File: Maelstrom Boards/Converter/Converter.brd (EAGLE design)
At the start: 101.6 x 101.6 mm, 1 part

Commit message: converter work
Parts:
- added 12VCONVERTER, 3.3VCONVERTER, 5VCONVERTER: CONVERTER, converter:CONVERTER
- added BALANCEDRAWIN: 39-30-06?, con-molex-mini-fit:39-30-?06?
- added C1, C12, C7: (no value), rcl:E3,5-10
- added C10, C13, C14, C15, C3, C4, C5, C8, C9: (no value), resistor:C1206K
- added C11, C2, C6: (no value), rcl:E5-13
- added DIAMOND: 43045-08, con-molex-micro-fit:43045-08
- added JETSON, PNUEMATICS: 39-30-02?, con-molex-mini-fit:39-30-?02?
- added L1, L2, L3: (no value), rcl:POWER-CHOKE_WE-TPC
- added Q1, Q2, Q3: BSS295, transistor-fet:TO92
- added R4: 4.47 K, rcl:0207/10
- added R5: 1.41 K, rcl:0207/10
- added R6: 7.6 K, rcl:0207/10
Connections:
- new net +12V: 12VCONVERTER.7,SENSE+, 12VCONVERTER.8,VOUT(+)
- new net +3V3: 3.3VCONVERTER.7,SENSE+, 3.3VCONVERTER.8,VOUT(+), U$1.4, U$1.5, U$1.51, U$1.52, U$1.53, U$1.6
- new net +5V: 5VCONVERTER.7,SENSE+, 5VCONVERTER.8,VOUT(+), U$1.1, U$1.2, U$1.3, U$1.54, U$1.55, U$1.56
- new net 12VCURRENTOUT: C3.1, C4.1, C5.1, DIAMOND.1, DIAMOND.2, DIAMOND.3, DIAMOND.4, JETSON.1, PNUEMATICS.1
- new net 12VFILTERED+: 12VCONVERTER.1,VIN(+)
- new net 12VON: Q1.1, U$1.21
- new net 3.3VFILTERED+: 3.3VCONVERTER.1,VIN(+)
- new net 3.3VON: Q3.1, U$1.23
- new net 5VFILTERED+: 5VCONVERTER.1,VIN(+)
- new net 5VON: Q2.1, U$1.22
- new net AGND: 12VCONVERTER.3,VIN(-)/GND, 12VCONVERTER.4,VOUT(-)/GND, 3.3VCONVERTER.3,VIN(-)/GND, 3.3VCONVERTER.4,VOUT(-)/GND, 5VCONVERTER.3,VIN(-)/GND, 5VCONVERTER.4,VOUT(-)/GND, Q1.3, Q2.3, Q3.3, R4.1, R5.1, R6.1, U$1.48, U$1.49, U$1.50, U$1.7, U$1.8, U$1.9
- new net BALANCED+: BALANCEDRAWIN.1, BALANCEDRAWIN.2, BALANCEDRAWIN.3, C1.+, C12.+, C7.+, L1.1, L2.1, L3.1
- new net BALANCED-: BALANCEDRAWIN.4, BALANCEDRAWIN.5, BALANCEDRAWIN.6, C1.-, C11.-, C12.-, C2.-, C6.-, C7.-
- new net CMGND: C3.2, C4.2, C5.2, DIAMOND.5, DIAMOND.6, DIAMOND.7, DIAMOND.8, JETSON.2, PNUEMATICS.2
- new net N$1: 5VCONVERTER.6,TRIM, R4.2
- new net N$10: C13.1, C14.1, C15.1
- new net N$11: C13.2, C14.2, C15.2
- new net N$13: 12VCONVERTER.2,ON/OFF, Q1.2
- new net N$16: 5VCONVERTER.2,ON/OFF, Q2.2
- new net N$17: 3.3VCONVERTER.6,TRIM, R6.2
- new net N$19: 3.3VCONVERTER.2,ON/OFF, Q3.2
- new net N$2: 12VCONVERTER.6,TRIM, R5.2
- new net N$3: C2.+, L1.2
- new net N$5: C6.+, L2.2
- new net N$6: C10.1, C8.1, C9.1
- new net N$7: C10.2, C8.2, C9.2
- new net N$9: C11.+, L3.2

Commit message: Converter work
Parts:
- added R1: 10K, rcl:R0603
- added R2: 1.41 K, rcl:R0603
- added R3, R7, R8, R9: 4.47 K, rcl:R0603
- C1, C7: value (none) -> 1000 uF
- C10, C13, C14, C15, C3, C4, C5, C8, C9: value (none) -> 47 uF
- C11, C2, C6: value (none) -> 330 uF; device rcl:E5-13 -> rcl:E3,5-8
- C12: value (none) -> 1000
- L1, L2, L3: value (none) -> 1 uH
- R4, R5, R6: device rcl:0207/10 -> rcl:R0603
- moved Q3 267.6 mm to (70.4, 82.3)
- moved Q1 264.1 mm to (70.1, 88.4)
- moved R6 263.2 mm to (79.8, 83.1)
- moved 12VCONVERTER 241.2 mm to (30.5, 71.1)
- moved R5 232.3 mm to (80.7, 47.3)
- moved R4 210.5 mm to (75.2, 58.9)
- moved Q2 206.2 mm to (82.6, 29.5)
- moved L3 173.5 mm to (83.2, 64.1)
- moved C7 172.9 mm to (7.83, 92.9)
- moved L1 170.7 mm to (24.6, 91.1), turned to 270 degrees
- moved 3.3VCONVERTER 168.6 mm to (30.5, 45.7)
- moved 5VCONVERTER 167.2 mm to (30.5, 20.3)
- moved C13 156.4 mm to (72.3, 43.7)
- moved C14 156.4 mm to (77.0, 43.7)
- moved C15 156.4 mm to (81.7, 43.7)
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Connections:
- net N$1 renamed 5VTRIM
- net N$10 renamed +3.3V
- net N$13 renamed 12VON-CON
- net N$16 renamed 5VON-CON
- net N$17 renamed 3.3VTRIM
- net N$19 renamed 3.3VON-CON
- net N$2 renamed 12VTRIM
- removed net 12VCURRENTOUT: C3.1, C4.1, C5.1, DIAMOND.1, DIAMOND.2, DIAMOND.3, DIAMOND.4, JETSON.1, PNUEMATICS.1
- removed net CMGND: C3.2, C4.2, C5.2, DIAMOND.5, DIAMOND.6, DIAMOND.7, DIAMOND.8, JETSON.2, PNUEMATICS.2
- removed net N$11: C13.2, C14.2, C15.2
- removed net N$3: C2.+, L1.2
- removed net N$5: C6.+, L2.2
- removed net N$6: C10.1, C8.1, C9.1
- removed net N$7: C10.2, C8.2, C9.2
- removed net N$9: C11.+, L3.2
- net +12V: now also C3.1, C4.1, C5.1, DIAMOND.1, DIAMOND.2, DIAMOND.3, DIAMOND.4, JETSON.1, PNUEMATICS.1
- net +5V: now also C10.1, C8.1, C9.1
- net 12VFILTERED+: now also C2.+, L1.2
- net 12VON: now also R1.1, R2.2
- net 3.3VFILTERED+: now also C11.+, L3.2
- net 3.3VON: now also R8.1, R9.2
- net 5VFILTERED+: now also C6.+, L2.2
- net 5VON: now also R3.1, R7.2
- net AGND: now also C10.2, C13.2, C14.2, C15.2, C3.2, C4.2, C5.2, C8.2, C9.2, DIAMOND.5, DIAMOND.6, DIAMOND.7, DIAMOND.8, JETSON.2, PNUEMATICS.2, R2.1, R7.1, R9.1
- net BALANCED+: now also R1.2, R3.2, R8.2

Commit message: Converter board
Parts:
- R2: value 1.41 K -> 1.35K
- R3, R8: value 4.47 K -> 10K
- R7, R9: value 4.47 K -> 1.35K
- moved R9 206.4 mm to (18.2, 57.7)
- moved R8 202.0 mm to (27.6, 57.1), turned to 90 degrees
- moved R2 193.8 mm to (19.0, 80.1), turned to 90 degrees
- moved R1 181.5 mm to (25.7, 79.6), turned to 270 degrees
- moved R7 171.0 mm to (28.9, 30.4)
- moved R3 158.0 mm to (24.3, 30.6), turned to 90 degrees
- moved DIAMOND 140.9 mm to (91.2, 68.5), turned to 90 degrees
- moved PNUEMATICS 136.4 mm to (87.4, 52.7), turned to 90 degrees
- moved JETSON 120.4 mm to (87.2, 84.8), turned to 90 degrees
- moved L2 60.8 mm to (22.4, 48.0), turned to 0 degrees
- moved L3 59.0 mm to (24.2, 63.5), turned to 180 degrees
- moved Q2 49.4 mm to (33.2, 30.6)
- moved Q3 44.1 mm to (34.8, 56.2)
- moved C7 42.0 mm to (8.24, 50.9), turned to 270 degrees
- moved Q1 36.1 mm to (35.1, 79.7)
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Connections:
- removed net BALANCED-: BALANCEDRAWIN.4, BALANCEDRAWIN.5, BALANCEDRAWIN.6, C1.-, C11.-, C12.-, C2.-, C6.-, C7.-
- net AGND: now also BALANCEDRAWIN.4, BALANCEDRAWIN.5, BALANCEDRAWIN.6, C1.-, C11.-, C12.-, C2.-, C6.-, C7.-
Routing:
- net AGND: track 0.00 -> 1.40 mm, vias 0 -> 1
- added copper zone on layer 16, net AGND
- added copper zone on layer 1, net BALANCED+

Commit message: Converter board work
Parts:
- moved R9 4.44 mm to (22.6, 57.2), turned to 270 degrees
- moved R2 1.37 mm to (20.2, 79.6)
- moved R7 0.83 mm to (28.1, 30.6), turned to 270 degrees
- moved Q1 0.76 mm to (34.4, 79.7)
- moved Q2 0.76 mm to (34.0, 30.6)
- moved Q3 0.51 mm to (34.3, 56.2)
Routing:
- net AGND: track 1.40 -> 5.37 mm, vias 1 -> 3

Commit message: Converter layout finished
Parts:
- moved C15 60.0 mm to (26.3, 20.8), turned to 180 degrees
- moved C10 57.7 mm to (18.9, 20.9), turned to 180 degrees
- moved C9 57.3 mm to (18.9, 17.6), turned to 180 degrees
- moved C14 57.0 mm to (26.3, 17.6), turned to 180 degrees
- moved C8 56.9 mm to (18.9, 14.3), turned to 180 degrees
- moved C13 54.6 mm to (26.3, 14.3), turned to 180 degrees
- moved C3 48.8 mm to (83.6, 62.3), turned to 180 degrees
- moved C4 47.7 mm to (83.6, 65.9), turned to 180 degrees
- moved C5 46.6 mm to (83.6, 69.4), turned to 180 degrees
- moved R5 36.8 mm to (75.4, 83.8), turned to 180 degrees
- moved R4 26.0 mm to (75.4, 32.9), turned to 180 degrees
- moved R6 25.1 mm to (75.4, 58.3), turned to 180 degrees
- moved R3 4.64 mm to (28.8, 31.4)
- moved L2 3.88 mm to (26.1, 46.6), turned to 90 degrees
- moved R2 3.31 mm to (23.5, 80.4), turned to 270 degrees
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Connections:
- removed net +3.3V: C13.1, C14.1, C15.1
- net +3V3: now also C13.1, C14.1, C15.1

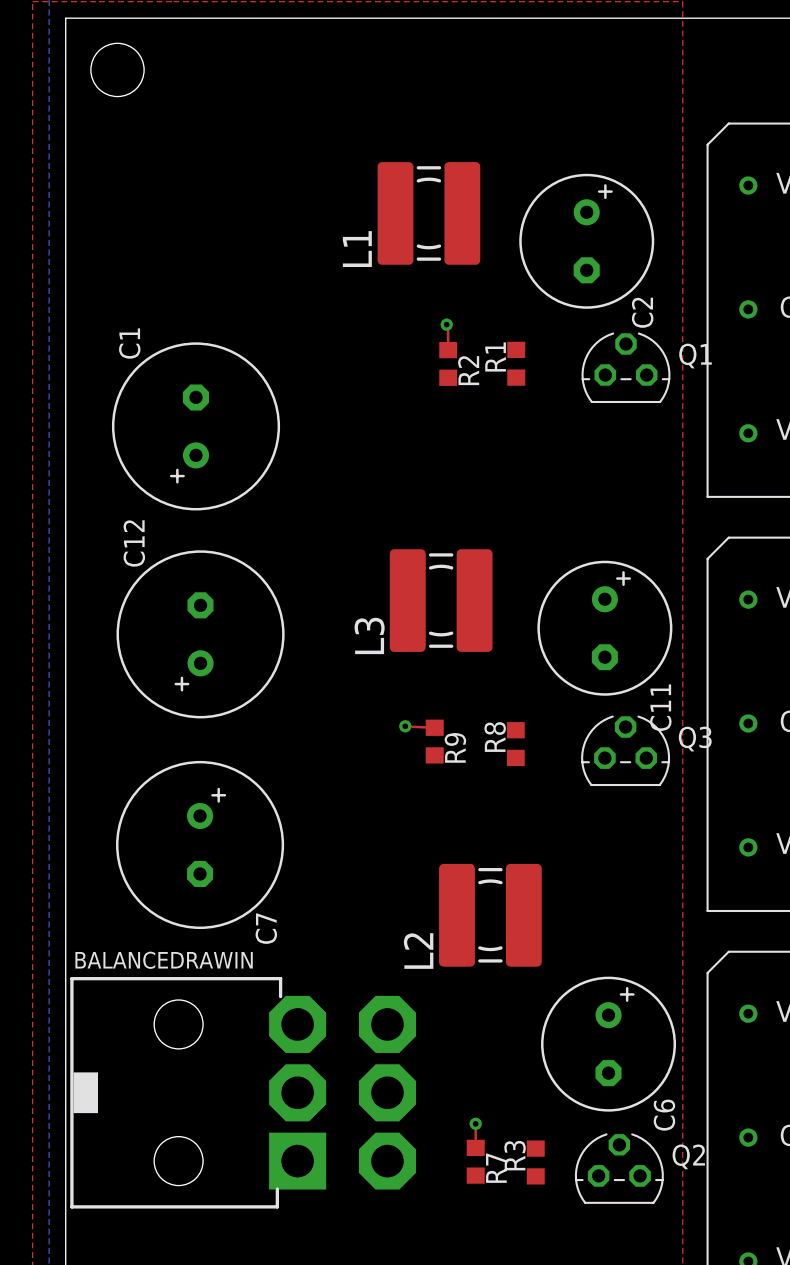
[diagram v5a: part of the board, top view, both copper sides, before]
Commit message: Changing converter board parts
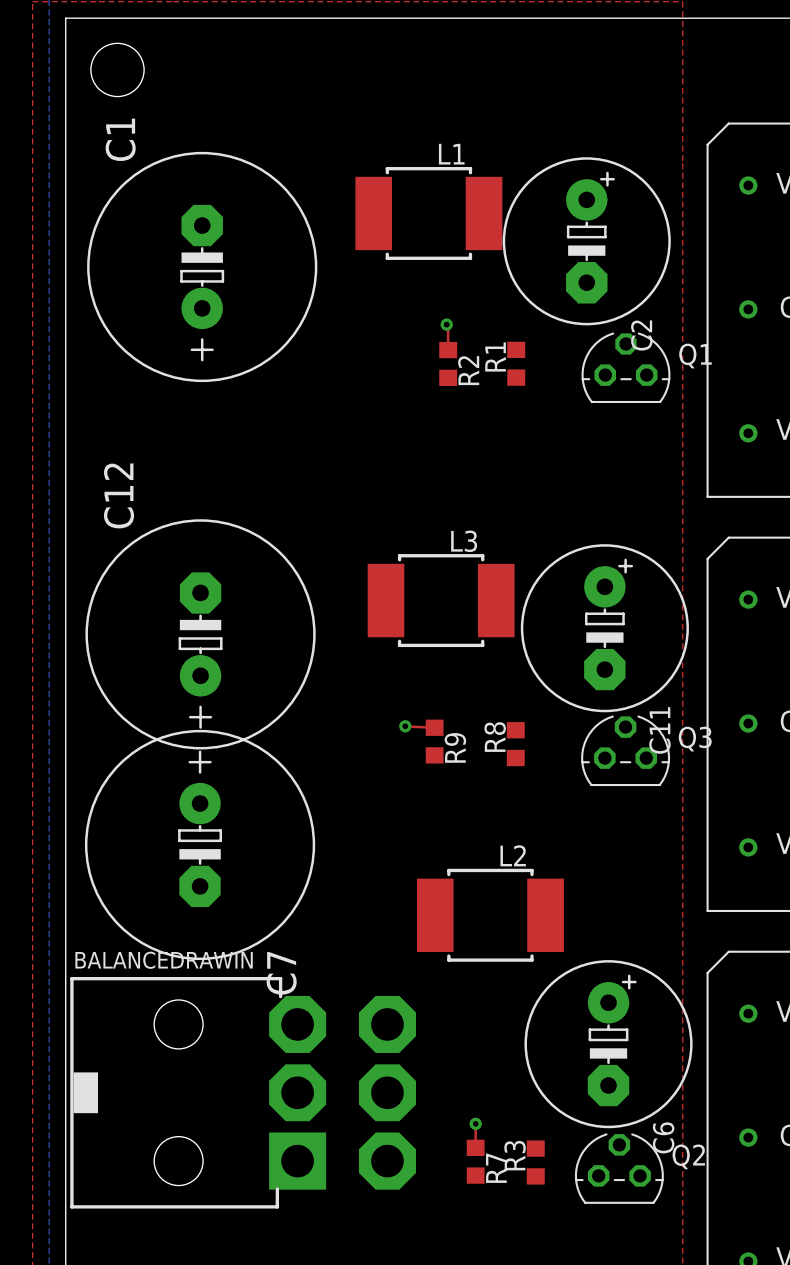
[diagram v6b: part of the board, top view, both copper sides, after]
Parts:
- C1, C12, C7: device rcl:E3,5-10 -> rcl:E5-13
- C11, C2, C6: device rcl:E3,5-8 -> rcl:E5-10,5
- L1, L2, L3: device rcl:POWER-CHOKE_WE-TPC -> inductor-neosid:MS85
- moved C1 9.79 mm to (8.37, 86.3)

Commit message: Changed values
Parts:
- R1, R3, R8: value 10K -> 100K
- R2, R7, R9: value 1.35K -> 13K
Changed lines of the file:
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@@
 <attribute name="SPICEPREFIX" value="C" x="33.0708" y="64.18071875" size="1.778" layer="27" rot="R270" display="off"/>
 </element>
-<element name="R1" library="rcl" library_urn="urn:adsk.eagle:library:334" package="R0603" package3d_urn="urn:adsk.eagle:package:23555/2" value="10K" x="27.6352" y="80.4046" rot="R90">
+<element name="R1" library="rcl" library_urn="urn:adsk.eagle:library:334" package="R0603" package3d_urn="urn:adsk.eagle:package:23555/2" value="100K" x="27.6352" y="80.4046" rot="R90">
 <attribute name="SPICEPREFIX" value="R" x="27.6352" y="80.4046" size="1.778" layer="27" rot="R90" display="off"/>
 </element>
-<element name="R2" library="rcl" library_urn="urn:adsk.eagle:library:334" package="R0603" package3d_urn="urn:adsk.eagle:package:23555/2" value="1.35K" x="23.456" y="80.391" rot="R270">
+<element name="R2" library="rcl" library_urn="urn:adsk.eagle:library:334" package="R0603" package3d_urn="urn:adsk.eagle:package:23555/2" value="13K" x="23.456" y="80.391" rot="R270">
 <attribute name="SPICEPREFIX" value="R" x="23.456" y="80.391" size="1.778" layer="27" rot="R270" display="off"/>
 </element>
-<element name="R3" library="rcl" library_urn="urn:adsk.eagle:library:334" package="R0603" package3d_urn="urn:adsk.eagle:package:23555/2" value="10K" x="28.829" y="31.408" rot="R90">
+<element name="R3" library="rcl" library_urn="urn:adsk.eagle:library:334" package="R0603" package3d_urn="urn:adsk.eagle:package:23555/2" value="100K" x="28.829" y="31.408" rot="R90">
 <attribute name="SPICEPREFIX" value="R" x="28.829" y="31.408" size="1.778" layer="27" rot="R90" display="off"/>
 </element>
-<element name="R7" library="rcl" library_urn="urn:adsk.eagle:library:334" package="R0603" package3d_urn="urn:adsk.eagle:package:23555/2" value="1.35K" x="25.146" y="31.457" rot="R270">
+<element name="R7" library="rcl" library_urn="urn:adsk.eagle:library:334" package="R0603" package3d_urn="urn:adsk.eagle:package:23555/2" value="13K" x="25.146" y="31.457" rot="R270">
 <attribute name="SPICEPREFIX" value="R" x="25.146" y="31.457" size="1.778" layer="27" rot="R270" display="off"/>
 </element>
-<element name="R8" library="rcl" library_urn="urn:adsk.eagle:library:334" package="R0603" package3d_urn="urn:adsk.eagle:package:23555/2" value="10K" x="27.6098" y="57.0738" rot="R90">
+<element name="R8" library="rcl" library_urn="urn:adsk.eagle:library:334" package="R0603" package3d_urn="urn:adsk.eagle:package:23555/2" value="100K" x="27.6098" y="57.0738" rot="R90">
 <attribute name="SPICEPREFIX" value="R" x="27.6098" y="57.0738" size="1.778" layer="27" rot="R90" display="off"/>
 </element>
-<element name="R9" library="rcl" library_urn="urn:adsk.eagle:library:334" package="R0603" package3d_urn="urn:adsk.eagle:package:23555/2" value="1.35K" x="22.6314" y="57.2262" rot="R270">
+<element name="R9" library="rcl" library_urn="urn:adsk.eagle:library:334" package="R0603" package3d_urn="urn:adsk.eagle:package:23555/2" value="13K" x="22.6314" y="57.2262" rot="R270">
 <attribute name="SPICEPREFIX" value="R" x="22.6314" y="57.2262" size="1.778" layer="27" rot="R270" display="off"/>
 </element>

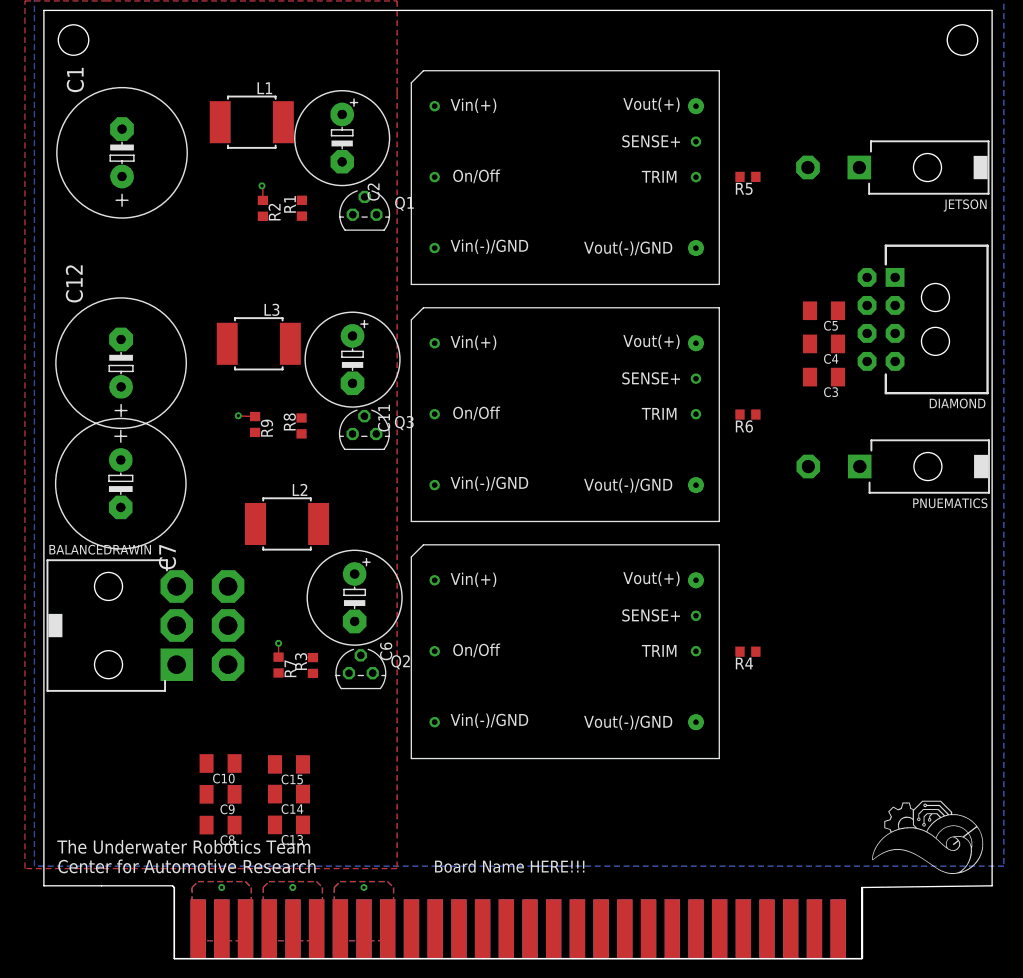
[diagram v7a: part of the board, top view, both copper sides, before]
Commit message: New schematic template and converter fixes
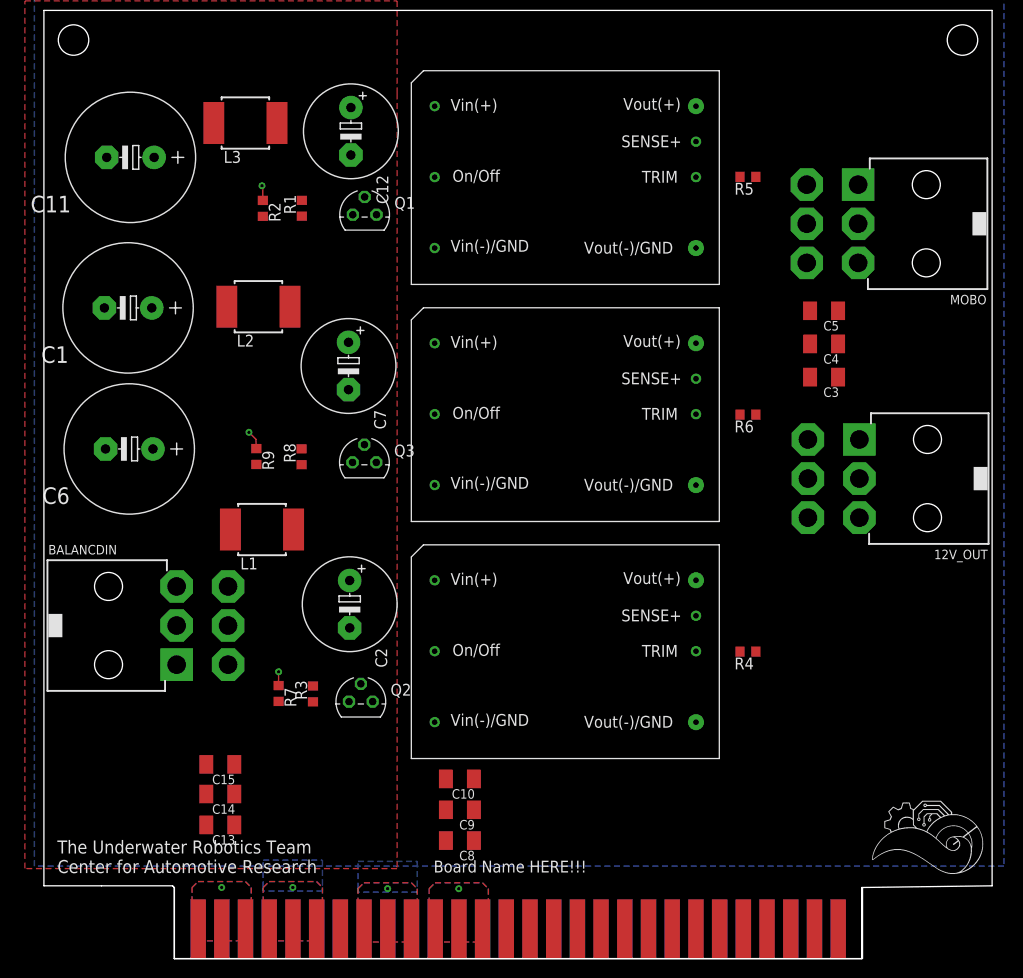
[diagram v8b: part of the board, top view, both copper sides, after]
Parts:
- removed DIAMOND: 43045-08, con-molex-micro-fit:43045-08
- removed JETSON, PNUEMATICS: 39-30-02?, con-molex-mini-fit:39-30-?02?
- added 12V_OUT, MOBO: (no value), con-molex-mini-fit:39-30-?06?
- BALANCDIN: value 39-30-06? -> (none)
- C11, C6: value 330 uF -> 1000 uF; device rcl:E5-10,5 -> rcl:E5-13
- C12: value 1000 -> 330 uF; device rcl:E5-13 -> rcl:E5-10,5
- C7: value 1000 uF -> 330 uF; device rcl:E5-13 -> rcl:E5-10,5
- moved C2 49.9 mm to (32.8, 38.0)
- moved L1 43.7 mm to (23.4, 46.0), turned to 270 degrees
- moved C12 35.0 mm to (32.9, 88.6), turned to 270 degrees
- moved C11 32.2 mm to (9.27, 85.9), turned to 180 degrees
- moved C6 28.9 mm to (9.14, 54.6), turned to 180 degrees
- moved C7 27.5 mm to (32.6, 63.5)
- moved C10 25.7 mm to (44.6, 19.3)
- moved C8 25.7 mm to (44.6, 12.6)
- moved C9 25.7 mm to (44.6, 16.0)
- moved L3 23.7 mm to (21.6, 89.5), turned to 270 degrees
- moved L2 23.5 mm to (23.0, 69.8), turned to 270 degrees
- moved C1 16.6 mm to (9.02, 69.7), turned to 180 degrees
- moved C13 7.37 mm to (18.9, 14.3)
- moved C14 7.37 mm to (18.9, 17.6)
- moved C15 7.37 mm to (18.9, 20.8)
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- renumbered BALANCEDRAWIN to BALANCDIN
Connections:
- net 12VTRIM renamed N$1
- net 3.3VTRIM renamed N$3
- net 5VTRIM renamed N$2
- removed net 12VFILTERED+: 12VCONVERTER.1,VIN(+), C2.+, L1.2
- removed net 3.3VFILTERED+: 3.3VCONVERTER.1,VIN(+), C11.+, L3.2
- removed net 5VFILTERED+: 5VCONVERTER.1,VIN(+), C6.+, L2.2
- removed net BALANCED+: BALANCDIN.1, BALANCDIN.2, BALANCDIN.3, C1.+, C12.+, C7.+, L1.1, L2.1, L3.1, R1.2, R3.2, R8.2
- new net 12VFILTERED: 12VCONVERTER.1,VIN(+), C12.+, L3.2
- new net 3.3VFILTERED: 3.3VCONVERTER.1,VIN(+), C7.+, L2.2
- new net 5VFILTERED: 5VCONVERTER.1,VIN(+), C2.+, L1.2
- new net V+: BALANCDIN.1, BALANCDIN.2, BALANCDIN.3, C1.+, C11.+, C6.+, L1.1, L2.1, L3.1, R1.2, R3.2, R8.2
- net +12V: now also 12V_OUT.1, 12V_OUT.2, 12V_OUT.3, MOBO.1, MOBO.2, MOBO.3; no longer DIAMOND.1, DIAMOND.2, DIAMOND.3, DIAMOND.4, JETSON.1, PNUEMATICS.1
- net +3V3: now also U$1.1, U$1.2, U$1.3, U$1.54, U$1.55, U$1.56; no longer U$1.4, U$1.5, U$1.51, U$1.52, U$1.53, U$1.6
- net +5V: now also U$1.11, U$1.12, U$1.13, U$1.44, U$1.45, U$1.46; no longer U$1.1, U$1.2, U$1.3, U$1.54, U$1.55, U$1.56
- net 12VON: now also U$1.16; no longer U$1.21
- net 3.3VON: now also U$1.14; no longer U$1.23
- net 5VON: now also U$1.15; no longer U$1.22
- net AGND: now also 12V_OUT.4, 12V_OUT.5, 12V_OUT.6, MOBO.4, MOBO.5, MOBO.6, U$1.10, U$1.4, U$1.47, U$1.5, U$1.51, U$1.52, U$1.53, U$1.6; no longer DIAMOND.5, DIAMOND.6, DIAMOND.7, DIAMOND.8, JETSON.2, PNUEMATICS.2, U$1.50, U$1.7
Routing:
- net AGND: track 5.06 -> 5.30 mm, vias 3 -> 5
- added copper zone on layer 1, net +3V3
- added copper zone on layer 16, net +3V3
- added copper zone on layer 1, net +5V
- added copper zone on layer 16, net +5V
- added copper zone on layer 1, net AGND
- added copper zone on layer 1, net V+
- removed copper zone on layer 1, net 3.3V
- removed copper zone on layer 16, net 3.3V
- removed copper zone on layer 1, net 5V
- removed copper zone on layer 16, net 5V
- removed copper zone on layer 1, net BALANCED+
- removed copper zone on layer 1, net GND
- removed copper zone on layer 16, net GND
